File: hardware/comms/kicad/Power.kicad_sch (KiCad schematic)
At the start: 10 parts

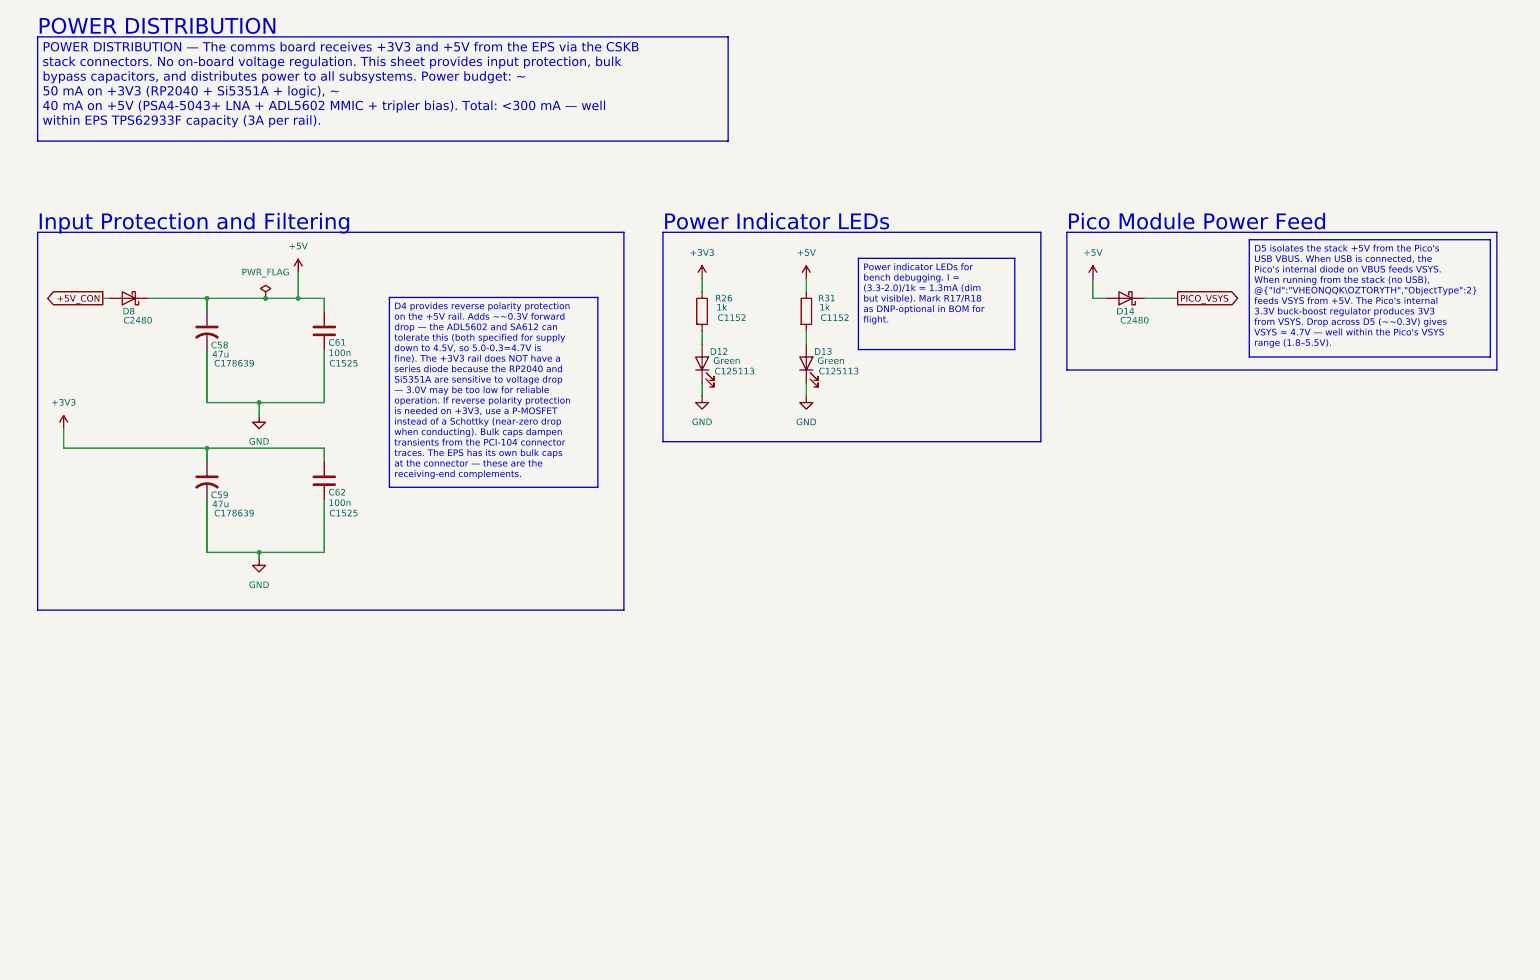
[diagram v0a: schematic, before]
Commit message: comms/kicad: rename project and sheets, correct schematic text
  Renames
  - transciever_kicad.{pro,sch,pcb} -> transceiver.{pro,sch,pcb}: the
    project name was misspelled, and the _kicad suffix was redundant
    inside a kicad/ directory.
  - Sheet files lose their spaces: Clock_Gen, Digital_Control, RX_Chain,
    TX_Chain. Sheetname keeps its space -- that is the label drawn on the
    sheet, not a path.
  - References updated in four places, not one: 4 Sheetfile properties in
    the root schematic, 186 per-symbol (project ...) instances across every
    sheet, 68 per-footprint (sheetfile ...) entries in the PCB, and
    meta.filename plus the root sheet name in the project file. Verified
    afterwards that all sheet references resolve, no sheet is orphaned, and
    the project file still parses.

  Spelling and stale labels
  - Title block: Revsion -> Revision, Repsoitory -> Repository, repository
    path centisat -> ember, project named EMBER.
  - PCI-104 -> CSKB in three files. PCI-104 is a different real standard,
    and the same sheet's own revision history records the bus being renamed
    to CSKB back at rev 0.4.
  - Status LED's -> Status LEDs; +20 db -> +20 dB; RX SMA < - -> <-.
  - The tripler note named BRF92A as the flight transistor: misspelled, and
    superseded by the 2SC3356 actually placed. Corrected to 2SC3356 with
    the MMBT3904-footprint note the implementation plan records. The
    ft=5 GHz figure is dropped rather than reassigned to a part it was not
    measured against.
  - Power sheet: the D4 forward-drop note referred to the SA612, replaced
    by the ADE-1+ back at rev 0.5. Now names the PSA4-5043+.
 Altium-to-KiCad text damage
  Three separate corruptions, classified before replacing so that real
  values were not caught up in it -- ~21 dB and ~20 dB both contain a
  literal ~2 and would have been mangled by a blind pass.
  - 144 table column separators rendered as literal ~2; now |, so the
    sheet index, rail summary, net c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
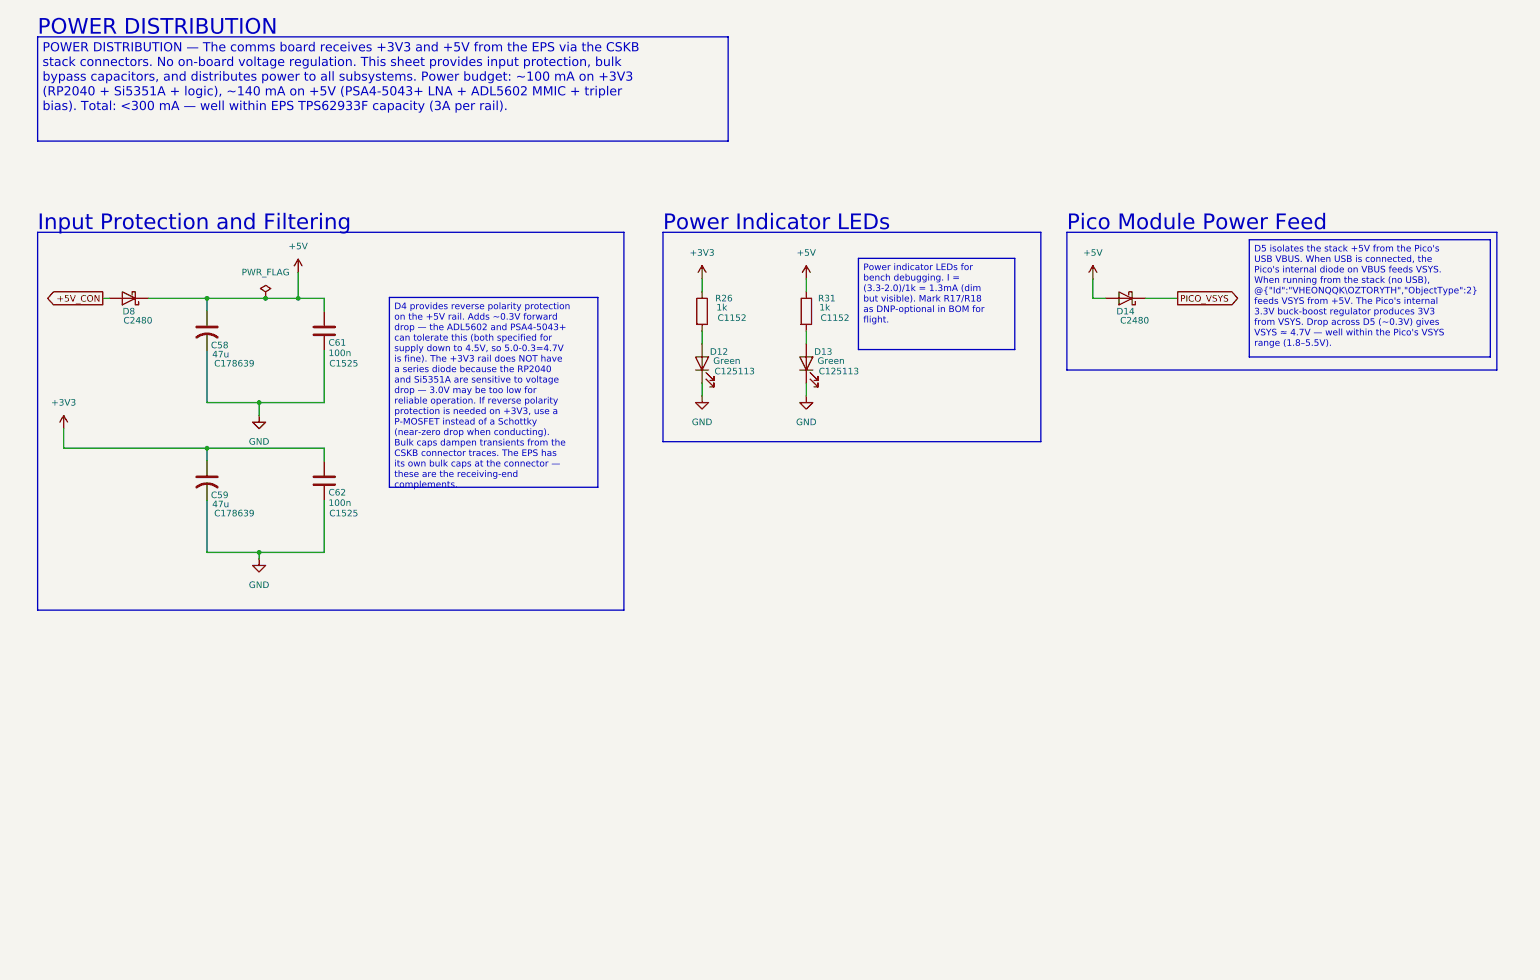
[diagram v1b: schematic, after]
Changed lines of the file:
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@@
 		)
 	)
-	(text_box "D5 isolates the stack +5V from the Pico's USB VBUS. When USB is connected, the Pico's internal diode on VBUS feeds VSYS. When running from the stack (no USB), @{\"Id\":\"VHEONQQK\\OZTORYTH\",\"ObjectType\":2} feeds VSYS from +5V. The Pico's internal 3.3V buck-boost regulator produces 3V3 from VSYS. Drop across D5 (~~0.3V) gives VSYS ≈ 4.7V — well within the Pico's VSYS range (1.8–5.5V)."
+	(text_box "D5 isolates the stack +5V from the Pico's USB VBUS. When USB is connected, the Pico's internal diode on VBUS feeds VSYS. When running from the stack (no USB), @{\"Id\":\"VHEONQQK\\OZTORYTH\",\"ObjectType\":2} feeds VSYS from +5V. The Pico's internal 3.3V buck-boost regulator produces 3V3 from VSYS. Drop across D5 (~0.3V) gives VSYS ≈ 4.7V — well within the Pico's VSYS range (1.8–5.5V)."
 		(exclude_from_sim no)
 		(at 279.4 80.01 0)
@@
 		)
 	)
-	(text_box "D4 provides reverse polarity protection on the +5V rail. Adds ~~0.3V forward drop — the ADL5602 and SA612 can tolerate this (both specified for supply down to 4.5V, so 5.0-0.3=4.7V is fine). The +3V3 rail does NOT have a series diode because the RP2040 and Si5351A are sensitive to voltage drop — 3.0V may be too low for reliable operation. If reverse polarity protection is needed on +3V3, use a P-MOSFET instead of a Schottky (near-zero drop when conducting). Bulk caps dampen transients from the PCI-104 connector traces. The EPS has its own bulk caps at the connector — these are the receiving-end complements."
+	(text_box "D4 provides reverse polarity protection on the +5V rail. Adds ~0.3V forward drop — the ADL5602 and PSA4-5043+ can tolerate this (both specified for supply down to 4.5V, so 5.0-0.3=4.7V is fine). The +3V3 rail does NOT have a series diode because the RP2040 and Si5351A are sensitive to voltage drop — 3.0V may be too low for reliable operation. If reverse polarity protection is needed on +3V3, use a P-MOSFET instead of a Schottky (near-zero drop when conducting). Bulk caps dampen transients from the CSKB connector traces. The EPS has its own bulk caps at the connector — these are the receiving-end complements."
 		(exclude_from_sim no)
 		(at 111.76 91.2622 0)
@@
 		)
 	)
-	(text_box "POWER DISTRIBUTION — The comms board receives +3V3 and +5V from the EPS via the CSKB stack connectors. No on-board voltage regulation. This sheet provides input protection, bulk bypass capacitors, and distributes power to all subsystems. Power budget: ~\n50 mA on +3V3 (RP2040 + Si5351A + logic), ~\n40 mA on +5V (PSA4-5043+ LNA + ADL5602 MMIC + tripler bias). Total: <300 mA — well within EPS TPS62933F capacity (3A per rail)."
+	(text_box "POWER DISTRIBUTION — The comms board receives +3V3 and +5V from the EPS via the CSKB stack connectors. No on-board voltage regulation. This sheet provides input protection, bulk bypass capacitors, and distributes power to all subsystems. Power budget: ~100 mA on +3V3 (RP2040 + Si5351A + logic), ~140 mA on +5V (PSA4-5043+ LNA + ADL5602 MMIC + tripler bias). Total: <300 mA — well within EPS TPS62933F capacity (3A per rail)."
 		(exclude_from_sim no)
 		(at 177.8 40.4622 0)
@@
 		)
 		(instances
-			(project "transciever_kicad"
+			(project "transceiver"
 				(path "/c034ea61-6551-4f92-af2a-65337e5cc22a/4f8afa8d-57f2-41d3-bba2-d581d8d3eaa2"
 					(reference "#PWR042")
@@
 		)
 		(instances
-			(project "transciever_kicad"
+			(project "transceiver"
 				(path "/c034ea61-6551-4f92-af2a-65337e5cc22a/4f8afa8d-57f2-41d3-bba2-d581d8d3eaa2"
 					(reference "C58")
@@
 		)
 		(instances
-			(project "transciever_kicad"
+			(project "transceiver"
 				(path "/c034ea61-6551-4f92-af2a-65337e5cc22a/4f8afa8d-57f2-41d3-bba2-d581d8d3eaa2"
 					(reference "C59")
@@
 		)
 		(instances
-			(project "transciever_kicad"
+			(project "transceiver"
 				(path "/c034ea61-6551-4f92-af2a-65337e5cc22a/4f8afa8d-57f2-41d3-bba2-d581d8d3eaa2"
 					(reference "#PWR087")
@@
 		)
 		(instances
-			(project "transciever_kicad"
+			(project "transceiver"
 				(path "/c034ea61-6551-4f92-af2a-65337e5cc22a/4f8afa8d-57f2-41d3-bba2-d581d8d3eaa2"
 					(reference "#PWR0101")
@@
 		)
 		(instances
-			(project "transciever_kicad"
+			(project "transceiver"
 				(path "/c034ea61-6551-4f92-af2a-65337e5cc22a/4f8afa8d-57f2-41d3-bba2-d581d8d3eaa2"
 					(reference "C61")
@@
 		)
 		(instances
-			(project "transciever_kicad"
+			(project "transceiver"
 				(path "/c034ea61-6551-4f92-af2a-65337e5cc22a/4f8afa8d-57f2-41d3-bba2-d581d8d3eaa2"
 					(reference "#FLG04")
@@
 		)
 		(instances
-			(project "transciever_kicad"
+			(project "transceiver"
 				(path "/c034ea61-6551-4f92-af2a-65337e5cc22a/4f8afa8d-57f2-41d3-bba2-d581d8d3eaa2"
 					(reference "#PWR040")
@@
 		)
 		(instances
-			(project "transciever_kicad"
+			(project "transceiver"
 				(path "/c034ea61-6551-4f92-af2a-65337e5cc22a/4f8afa8d-57f2-41d3-bba2-d581d8d3eaa2"
 					(reference "R31")
@@
 		)
 		(instances
-			(project "transciever_kicad"
+			(project "transceiver"
 				(path "/c034ea61-6551-4f92-af2a-65337e5cc22a/4f8afa8d-57f2-41d3-bba2-d581d8d3eaa2"
 					(reference "#PWR0100")
@@
 		)
 		(instances
-			(project "transciever_kicad"
+			(project "transceiver"
 				(path "/c034ea61-6551-4f92-af2a-65337e5cc22a/4f8afa8d-57f2-41d3-bba2-d581d8d3eaa2"
 					(reference "#PWR032")
@@
 		)
 		(instances
-			(project "transciever_kicad"
+			(project "transceiver"
 				(path "/c034ea61-6551-4f92-af2a-65337e5cc22a/4f8afa8d-57f2-41d3-bba2-d581d8d3eaa2"
 					(reference "D12")
@@
 		)
 		(instances
-			(project "transciever_kicad"
+			(project "transceiver"
 				(path "/c034ea61-6551-4f92-af2a-65337e5cc22a/4f8afa8d-57f2-41d3-bba2-d581d8d3eaa2"
 					(reference "D13")
@@
 		)
 		(instances
-			(project "transciever_kicad"
+			(project "transceiver"
 				(path "/c034ea61-6551-4f92-af2a-65337e5cc22a/4f8afa8d-57f2-41d3-bba2-d581d8d3eaa2"
 					(reference "D14")
@@
 		)
 		(instances
-			(project "transciever_kicad"
+			(project "transceiver"
 				(path "/c034ea61-6551-4f92-af2a-65337e5cc22a/4f8afa8d-57f2-41d3-bba2-d581d8d3eaa2"
 					(reference "#PWR088")
@@
 		)
 		(instances
-			(project "transciever_kicad"
+			(project "transceiver"
 				(path "/c034ea61-6551-4f92-af2a-65337e5cc22a/4f8afa8d-57f2-41d3-bba2-d581d8d3eaa2"
 					(reference "D8")
@@
 		)
 		(instances
-			(project "transciever_kicad"
+			(project "transceiver"
 				(path "/c034ea61-6551-4f92-af2a-65337e5cc22a/4f8afa8d-57f2-41d3-bba2-d581d8d3eaa2"
 					(reference "#PWR0111")
@@
 		)
 		(instances
-			(project "transciever_kicad"
+			(project "transceiver"
 				(path "/c034ea61-6551-4f92-af2a-65337e5cc22a/4f8afa8d-57f2-41d3-bba2-d581d8d3eaa2"
 					(reference "#PWR038")
@@
 		)
 		(instances
-			(project "transciever_kicad"
+			(project "transceiver"
 				(path "/c034ea61-6551-4f92-af2a-65337e5cc22a/4f8afa8d-57f2-41d3-bba2-d581d8d3eaa2"
 					(reference "C62")
@@
 		)
 		(instances
-			(project "transciever_kicad"
+			(project "transceiver"
 				(path "/c034ea61-6551-4f92-af2a-65337e5cc22a/4f8afa8d-57f2-41d3-bba2-d581d8d3eaa2"
 					(reference "R26")

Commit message: comms: checkpoint current KiCad design before ground station work
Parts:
- C58, C59: footprint (none) -> Ember_RF:CP_Elec_Panasonic_D_6.3x5.8; symbol Device:C_US -> Device:C_Polarized_US; MPN (none) -> EEHZA1V470P; Manufacturer (none) -> Panasonic; Voltage (none) -> 35V
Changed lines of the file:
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@@
 		(title "CubeSat Comms -- Power")
 		(rev "A")
+		(comment 9 "UHF/UHF revision in review - not for fabrication")
 	)
 	(rectangle
@@
 	)
 	(symbol
-		(lib_id "Device:C_US")
+		(lib_id "Device:C_Polarized_US")
 		(at 76.2 97.79 0)
 		(unit 1)
@@
 			)
 		)
-		(property "Footprint" ""
+		(property "Footprint" "Ember_RF:CP_Elec_Panasonic_D_6.3x5.8"
 			(at 76.2 97.79 0)
 			(hide yes)
@@
 			)
 		)
-		(property "Datasheet" ""
+		(property "Datasheet" "https://industrial.panasonic.com/content/data/CP/PDF/news2014/en/VH_E.pdf"
 			(at 76.2 97.79 0)
 			(hide yes)
@@
 			)
 		)
-		(property "Description" "capacitor, US symbol"
+		(property "Description" "47uF 35V polarized hybrid aluminum electrolytic; ZA size D"
 			(at 76.2 97.79 0)
 			(hide yes)
@@
 		(property "LCSC Part #" "C178639"
 			(at 81.534 104.14 0)
+			(show_name no)
+			(do_not_autoplace no)
+			(effects
+				(font
+					(size 1.27 1.27)
+				)
+			)
+		)
+		(property "MPN" "EEHZA1V470P"
+			(at 76.2 97.79 0)
+			(hide yes)
+			(show_name no)
+			(do_not_autoplace no)
+			(effects
+				(font
+					(size 1.27 1.27)
+				)
+			)
+		)
+		(property "Manufacturer" "Panasonic"
+			(at 76.2 97.79 0)
+			(hide yes)
+			(show_name no)
+			(do_not_autoplace no)
+			(effects
+				(font
+					(size 1.27 1.27)
+				)
+			)
+		)
+		(property "Voltage" "35V"
+			(at 76.2 97.79 0)
+			(hide yes)
 			(show_name no)
 			(do_not_autoplace no)
@@
 	)
 	(symbol
-		(lib_id "Device:C_US")
+		(lib_id "Device:C_Polarized_US")
 		(at 76.2 127 0)
 		(unit 1)
@@
 			)
 		)
-		(property "Footprint" ""
+		(property "Footprint" "Ember_RF:CP_Elec_Panasonic_D_6.3x5.8"
 			(at 76.2 127 0)
 			(hide yes)
@@
 			)
 		)
-		(property "Datasheet" ""
+		(property "Datasheet" "https://industrial.panasonic.com/content/data/CP/PDF/news2014/en/VH_E.pdf"
 			(at 76.2 127 0)
 			(hide yes)
@@
 			)
 		)
-		(property "Description" "capacitor, US symbol"
+		(property "Description" "47uF 35V polarized hybrid aluminum electrolytic; ZA size D"
 			(at 76.2 127 0)
 			(hide yes)
@@
 			(show_name no)
 			(do_not_autoplace no)
+			(effects
+				(font
+					(size 1.27 1.27)
+				)
+			)
+		)
+		(property "MPN" "EEHZA1V470P"
+			(at 76.2 127 0)
+			(hide yes)
+			(show_name no)
+			(do_not_autoplace no)
+			(effects
+				(font
+					(size 1.27 1.27)
+				)
+			)
+		)
+		(property "Manufacturer" "Panasonic"
+			(at 76.2 127 0)
+			(hide yes)
+			(show_name no)
+			(do_not_autoplace no)
+			(effects
+				(font
+					(size 1.27 1.27)
+				)
+			)
+		)
+		(property "Voltage" "35V"
+			(at 76.2 127 0)
+			(hide yes)
+			(show_name no)
+			(do_not_autoplace no)

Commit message: Complete dual-CAN transceiver hardware prototype
Preserve the current transceiver schematics, PCB, libraries and validation evidence as a focused hardware review against main.
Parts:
- removed D8: D_Schottky, Diode_SMD:D_SMA, symbol Device:D_Schottky
- added C116: 10nF, Capacitor_SMD:C_0603_1608Metric, symbol Device:C
- added C117, C118: 1uF, Capacitor_SMD:C_0603_1608Metric, symbol Device:C
- added R46: 470k, Resistor_SMD:R_0603_1608Metric, symbol Device:R
- added U15: LM73100RPWR, Ember_RF:Texas_RPW0010A_VQFN-HR-10_2x2mm, symbol Ember_RF:LM73100RPWR
- D12, D13: LCSC Part # C125113 -> C125094; MPN (none) -> LTST-C190KGKT; Manufacturer (none) -> Lite-On
- R26, R31: LCSC Part # C1152 -> C11702; MPN (none) -> 0402WGF1001TCE; Manufacturer (none) -> UNI-ROYAL(Uniroyal Elec); Manufacturer Part # (none) -> 0402WGF1001TCE
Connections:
- net +5V: now also C118.1, U15.6 (OUT)
- net +5V_CON: now also C117.1, R46.1, U15.5 (IN)
- net GND: now also C116.2, C117.2, C118.2, U15.2 (OVLO), U15.4 (PGTH), U15.8 (GND), U15.9 (IMON)
- new net PWR_DVDT: C116.1, U15.7 (DVDT)
- new net PWR_EN: R46.2, U15.1 (EN/UVLO)
- no-connect marks 0 -> 2
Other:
- note added: "+5V supplied through U15 below. C58/C61 provide bulk and high-frequency bypass. +3V3 comes directly from EPS. C59/C62 provide bypass."
- note added: "5V Input Protection / Controlled Turn-On"
- note added: "D14 isolates the Pico VSYS feed from USB-powered VSYS. Retain this Schottky diode. Pico VSYS range: 1.8 to 5.5 V."
- note added: "The comms board receives +3V3 and +5V_CON from the EPS stack connectors. U15 provides low-loss reverse-current blocking and controlled turn-on for +5V. Bulk capacitors and local bypass capacitors filter the distributed rails. Verify at least 4.5 V at the CAN controllers and RF amplifier under maximum load. Qualify the complete system current budget, ripple and transients before flight."
- note added: "U15 replaces D8: reverse-current blocking and low forward loss. R46 enables from +5V_CON; C116 sets about 25 ms turn-on at 5 V. C117/C118 are local bypass capacitors. Place close to U15. Pins 2, 4 and 9 tied to GND; PG unused; DNC pad 10 isolated. No copper beyond DNC land. No low-current overload protection."
